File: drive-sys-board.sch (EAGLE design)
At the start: 28 parts, among them J2 APP_2POS_CONFIG12V_HORIZ, U1 OKI-78SR-5/1.5-W36HC, U2 MAX232, U3 MAX232, U4 MAX232

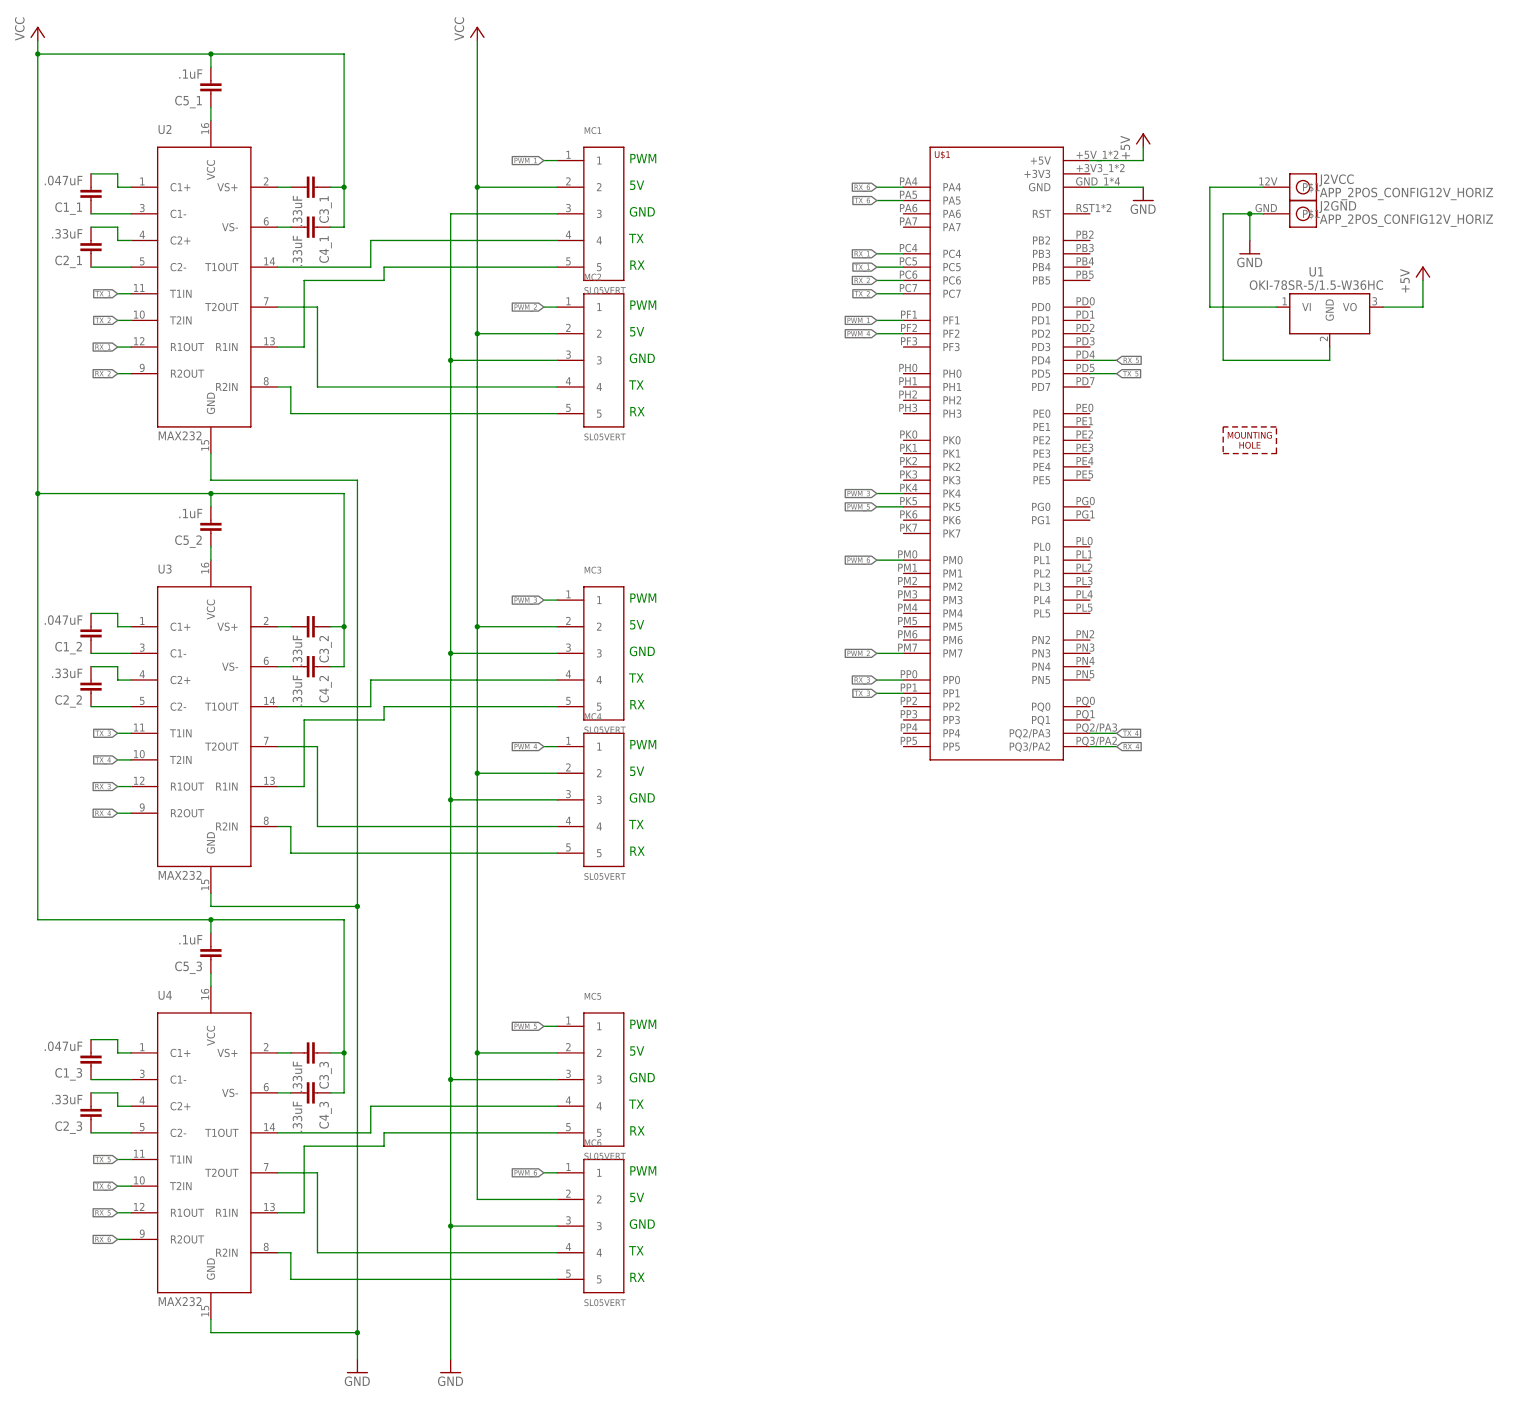
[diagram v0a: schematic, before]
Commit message: Made slight changes to prepare for board review
- Added decoupling capacitors to OKI
- Replaced VCC supply symbol with +5V
- Disconnected +5V from capacitors (let them connect to +5V plane)
- Swap connectors 3 and 4 to create progression from right to left
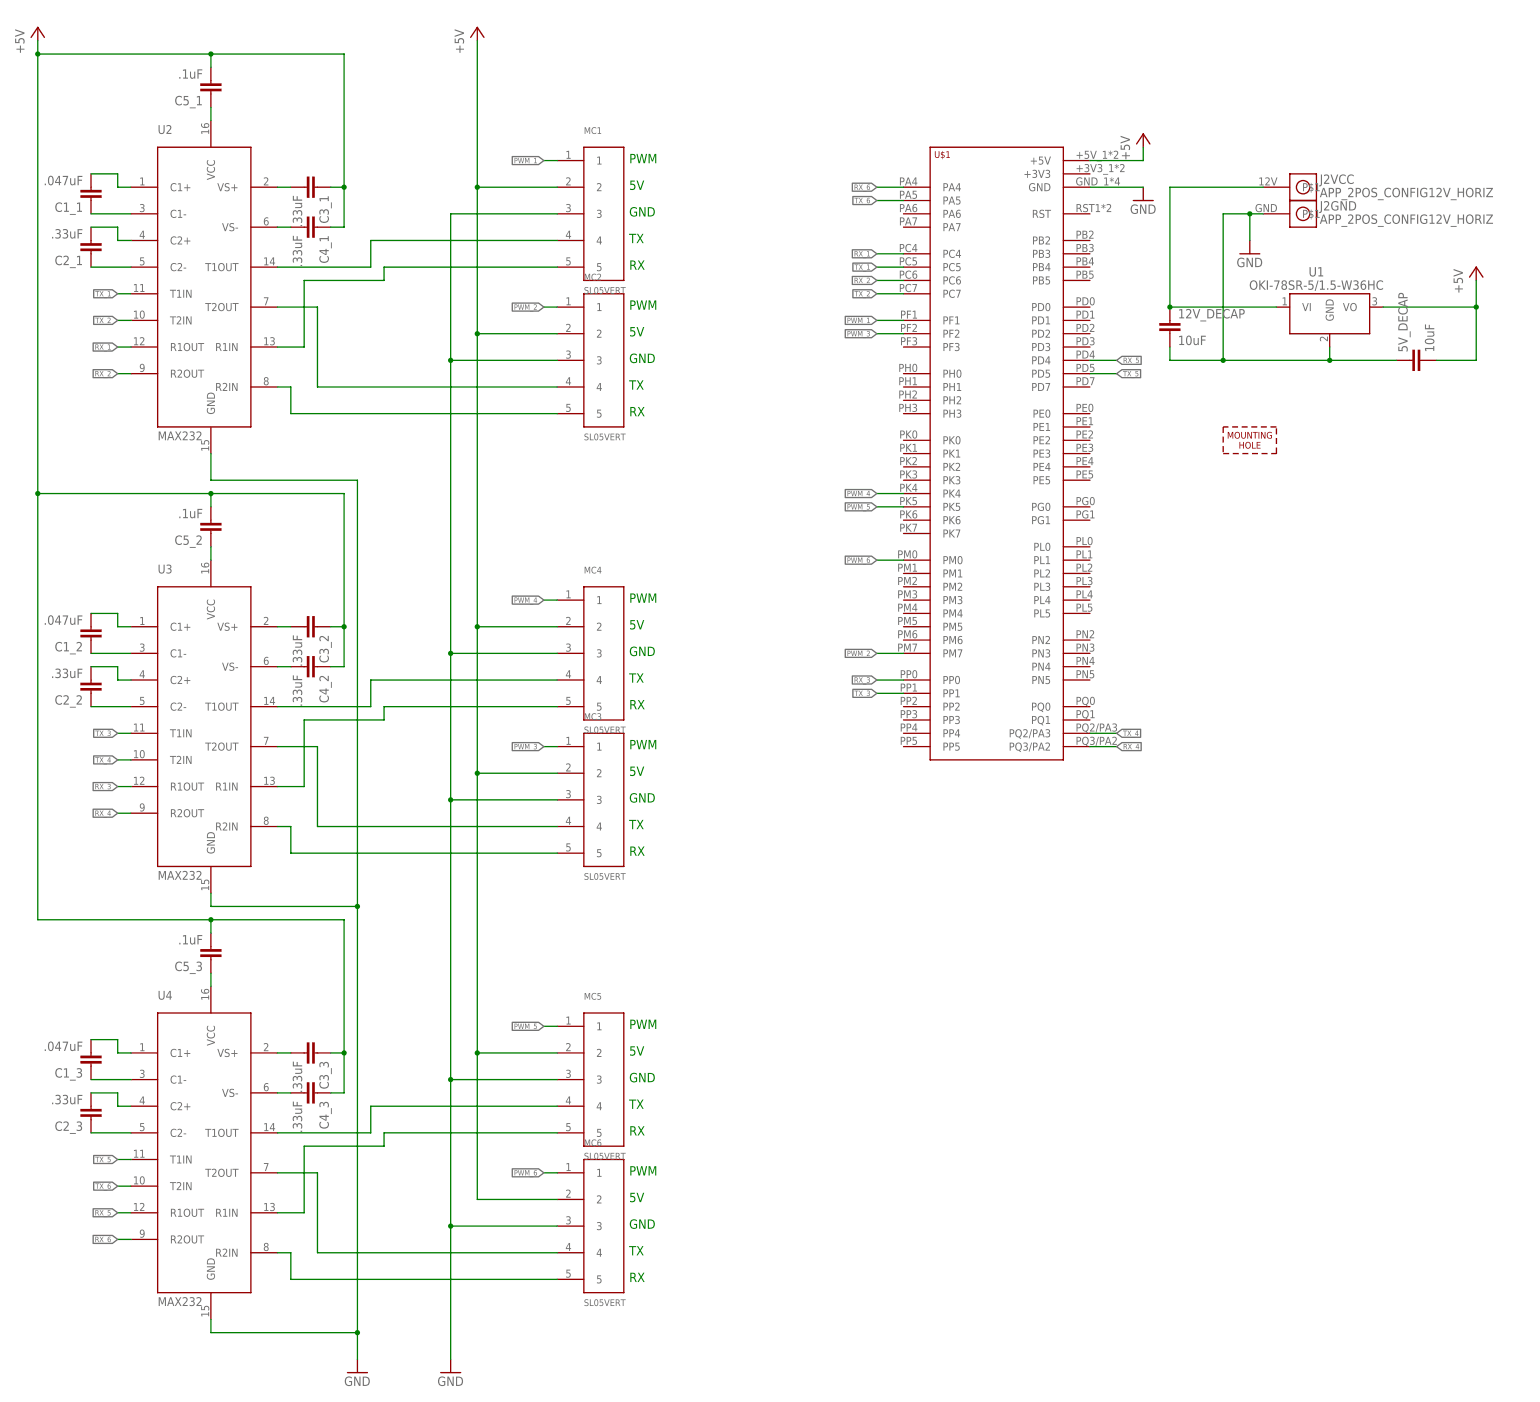
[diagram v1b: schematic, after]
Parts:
- added 12V_DECAP, 5V_DECAP: 10uF, SparkFun-Capacitors:CAP1206
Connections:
- removed net VCC: C3_1.1, C3_2.1, C3_3.1, C4_1.1, C4_2.1, C4_3.1, C5_1.2, C5_2.2, C5_3.2, MC1.2, MC2.2, MC3.2, MC4.2, MC5.2, MC6.2
- net +5V: now also 5V_DECAP.2, C3_1.1, C3_2.1, C3_3.1, C4_1.1, C4_2.1, C4_3.1, C5_1.2, C5_2.2, C5_3.2, MC1.2, MC2.2, MC3.2, MC4.2, MC5.2, MC6.2
- net GND: now also 12V_DECAP.2, 5V_DECAP.1
- net N$30: now also MC3.5; no longer MC4.5
- net N$31: now also MC3.4; no longer MC4.4
- net N$32: now also MC4.4; no longer MC3.4
- net N$33: now also MC4.5; no longer MC3.5
- net N$5: now also 12V_DECAP.1
- net PWM_3: now also U$1.PF2; no longer U$1.PK4
- net PWM_4: now also U$1.PK4; no longer U$1.PF2
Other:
- moved on the sheet: MC3, MC4

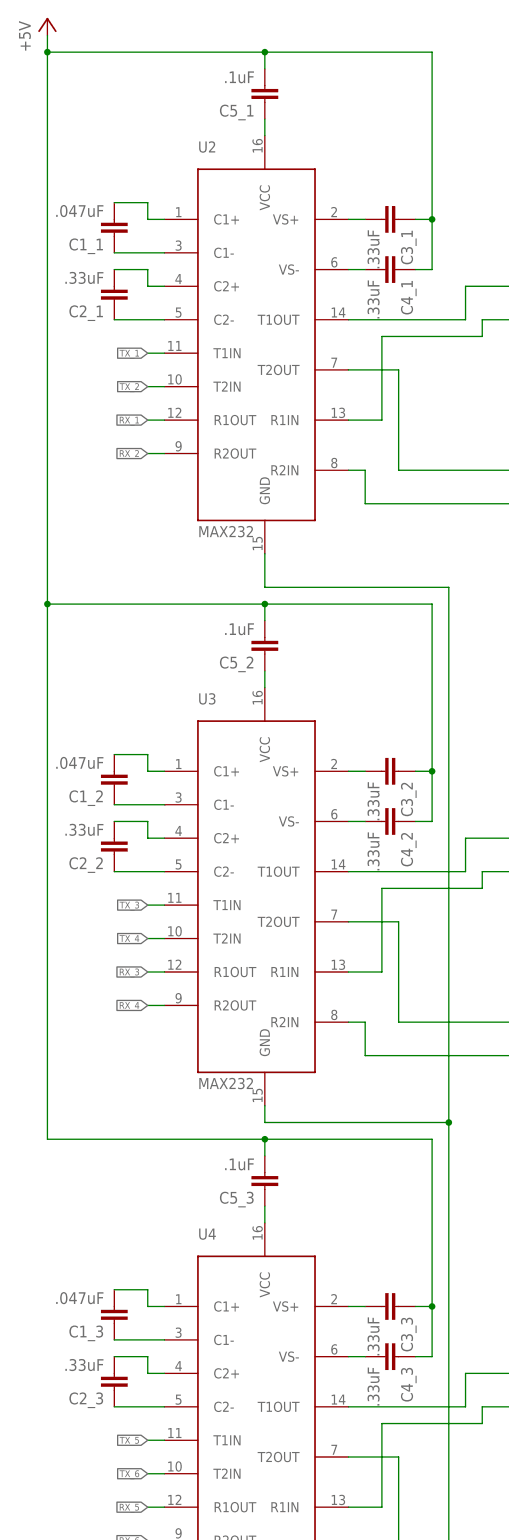
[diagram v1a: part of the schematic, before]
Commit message: Made changes from Drive Board Review 2
- Widened SL Connector Spacing
- Set all MAX232 Capacitors to 1uF, as shown in MAX232 datasheet
- Changed all capacitors from 1206 to 0805
- Increased silkscreen label size
- Added labels for motor position (ex: Front Left, Middle Left, etc)
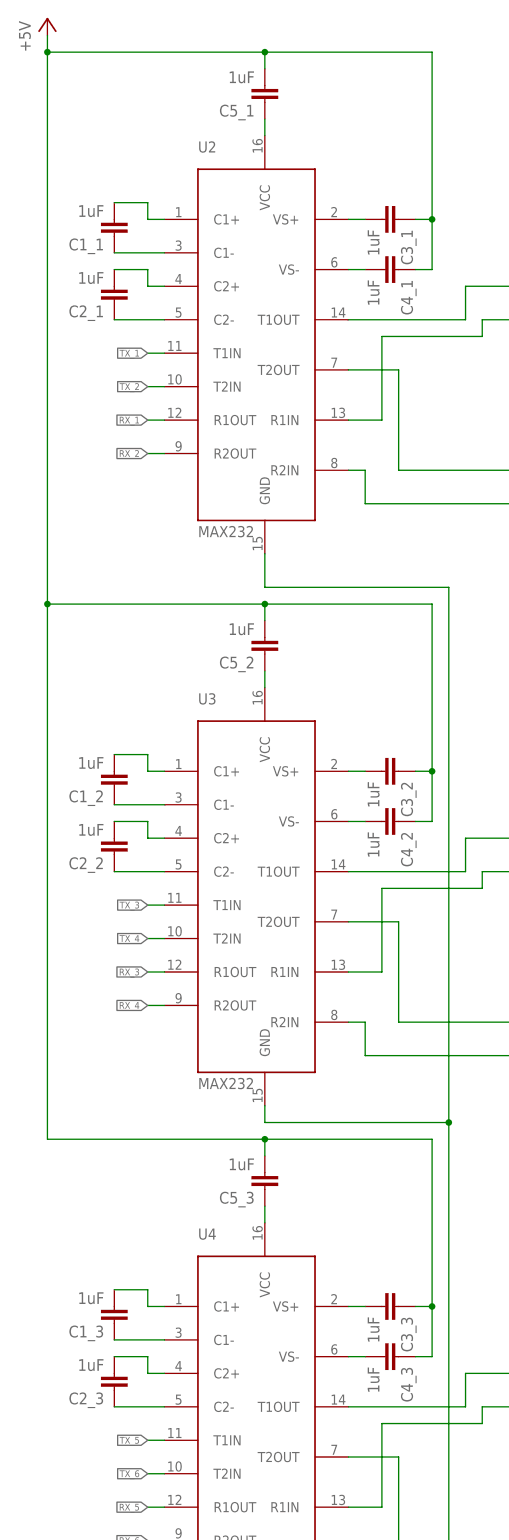
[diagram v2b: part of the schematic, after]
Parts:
- 12V_DECAP, 5V_DECAP: device SparkFun-Capacitors:CAP1206 -> SparkFun-Capacitors:CAP0805
- C1_1, C1_2, C1_3: value .047uF -> 1uF; device SparkFun-Capacitors:CAP1206 -> SparkFun-Capacitors:CAP0805
- C2_1, C2_2, C2_3, C3_1, C3_2, C3_3, C4_1, C4_2, C4_3: value .33uF -> 1uF; device SparkFun-Capacitors:CAP1206 -> SparkFun-Capacitors:CAP0805
- C5_1, C5_2, C5_3: value .1uF -> 1uF; device SparkFun-Capacitors:CAP1206 -> SparkFun-Capacitors:CAP0805

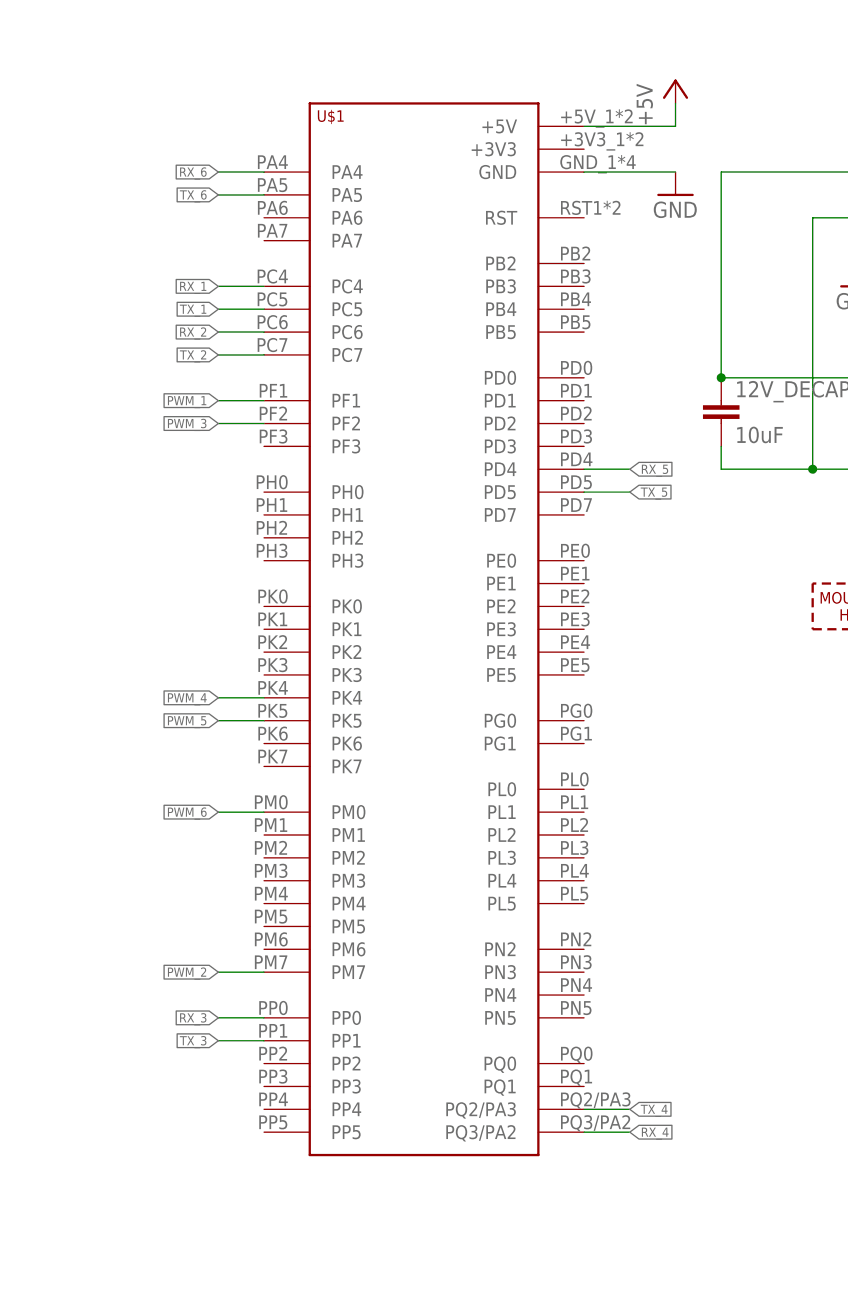
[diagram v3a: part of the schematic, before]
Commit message: Changed serial pairs to match Tiva hardware
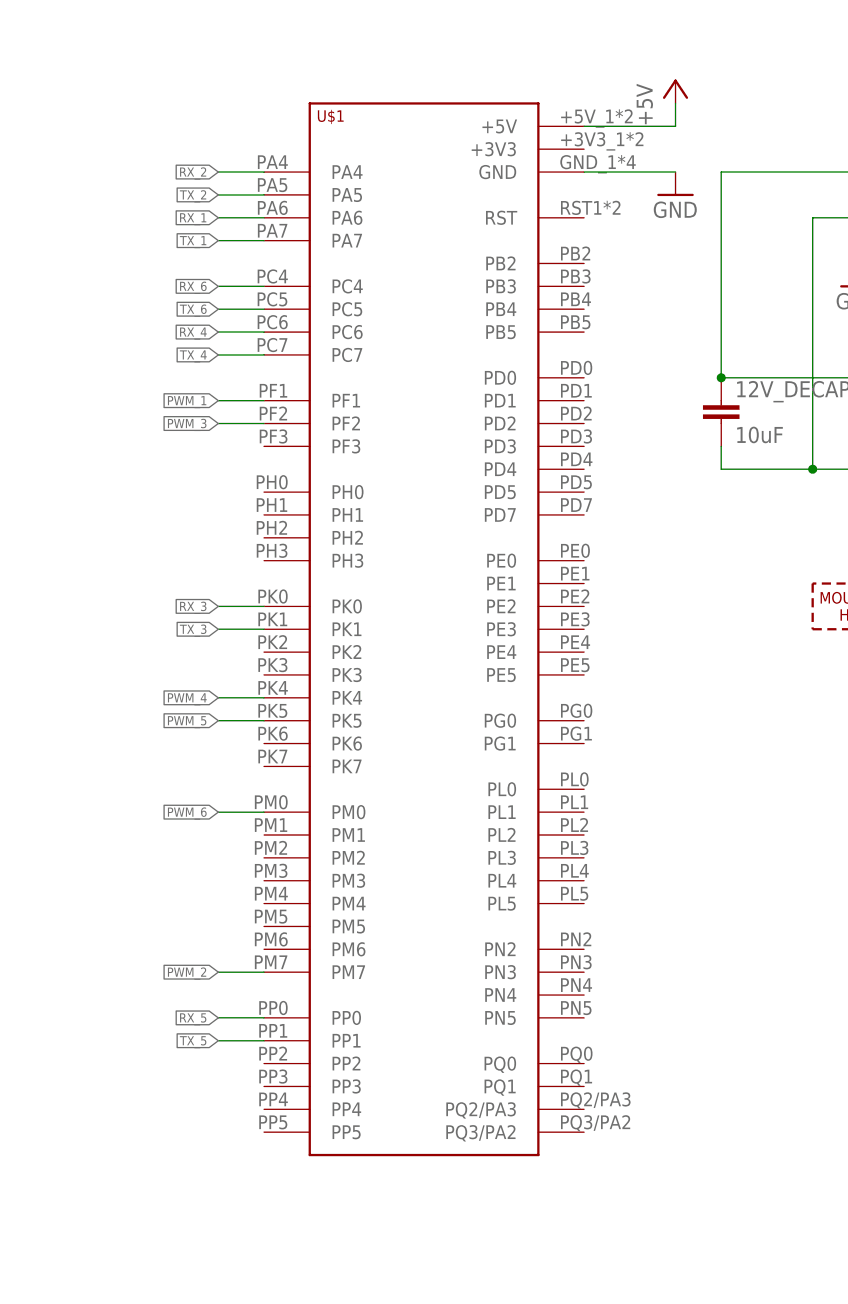
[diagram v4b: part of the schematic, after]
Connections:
- net RX_1: now also U$1.PA6; no longer U$1.PC4
- net RX_2: now also U$1.PA4; no longer U$1.PC6
- net RX_3: now also U$1.PK0; no longer U$1.PP0
- net RX_4: now also U$1.PC6; no longer U$1.PQ3/PA2
- net RX_5: now also U$1.PP0; no longer U$1.PD4
- net RX_6: now also U$1.PC4; no longer U$1.PA4
- net TX_1: now also U$1.PA7; no longer U$1.PC5
- net TX_2: now also U$1.PA5; no longer U$1.PC7
- net TX_3: now also U$1.PK1; no longer U$1.PP1
- net TX_4: now also U$1.PC7; no longer U$1.PQ2/PA3
- net TX_5: now also U$1.PP1; no longer U$1.PD5
- net TX_6: now also U$1.PC5; no longer U$1.PA5
